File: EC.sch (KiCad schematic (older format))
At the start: 9 parts, among them J2 MICROSD, J8 DEBUG, Q3 2N7002

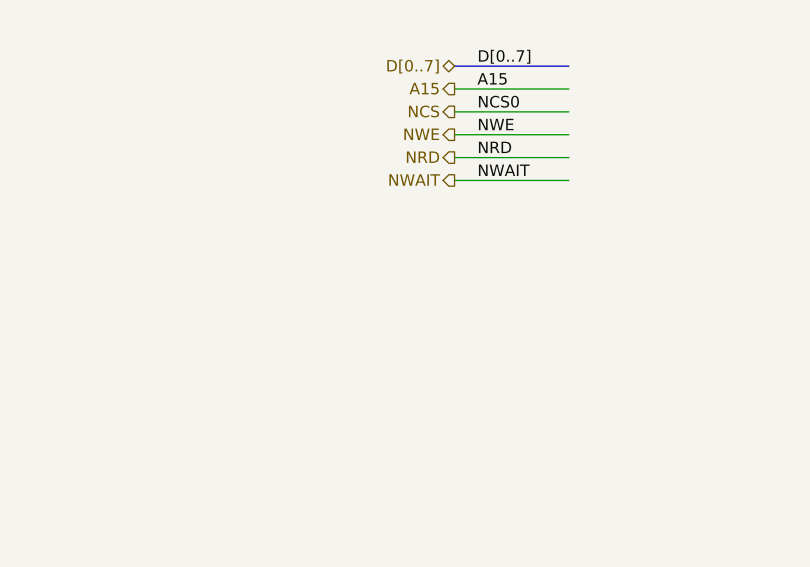
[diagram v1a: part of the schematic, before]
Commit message: Route CPU bus and cache
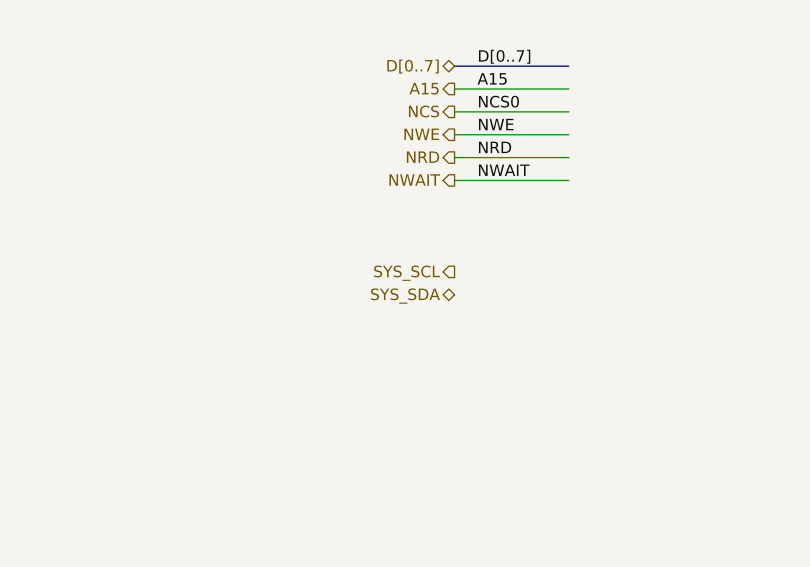
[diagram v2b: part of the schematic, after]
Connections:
- net labels added: SYS_SCL, SYS_SDA
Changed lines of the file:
@@
 $Descr A4 11693 8268
 encoding utf-8
-Sheet 7 9
+Sheet 6 9
 Title ""
 Date ""
@@
 Connection ~ 6800 1400
 $Comp
-L GND #PWR108
+L GND #PWR118
 U 1 1 577B8084
 P 6800 1500
-F 0 "#PWR108" H 6800 1500 30  0001 C CNN
+F 0 "#PWR118" H 6800 1500 30  0001 C CNN
 F 1 "GND" H 6800 1430 30  0001 C CNN
 F 2 "" H 6800 1500 60  0000 C CNN
@@
 $EndComp
 $Comp
-L GND #PWR109
+L GND #PWR119
 U 1 1 577B80BD
 P 7400 2400
-F 0 "#PWR109" H 7400 2400 30  0001 C CNN
+F 0 "#PWR119" H 7400 2400 30  0001 C CNN
 F 1 "GND" H 7400 2330 30  0001 C CNN
 F 2 "" H 7400 2400 60  0000 C CNN
@@
 	7000 1100 7000 1850
 Connection ~ 7000 1100
-$Comp
-L 2N7002 Q3
-U 1 1 577AFC0B
-P 8050 850
-F 0 "Q3" H 8177 896 50  0000 L CNN
-F 1 "2N7002" H 8177 805 50  0000 L CNN
-F 2 "smd-semi:SOT-23" H 8050 700 50  0001 C CNN
-F 3 "" H 8050 850 60  0000 C CNN
-F 4 "NMOS 2N7002" H 8050 600 60  0001 C CNN "BOM"
-	1    8050 850
-	1    0    0    -1
-$EndComp
 Text GLabel 7950 700  0    50   Input ~ 0
 3V3_LIMB
@@
 	8100 950  8100 1200
 $Comp
-L GND #PWR110
+L GND #PWR120
 U 1 1 577B0609
 P 8100 1450
-F 0 "#PWR110" H 8100 1450 30  0001 C CNN
+F 0 "#PWR120" H 8100 1450 30  0001 C CNN
 F 1 "GND" H 8100 1380 30  0001 C CNN
 F 2 "" H 8100 1450 60  0000 C CNN
@@
 	10600 5800 10500 5800
 $Comp
-L GND #PWR111
+L GND #PWR121
 U 1 1 577EAB82
 P 10600 6800
-F 0 "#PWR111" H 10600 6800 30  0001 C CNN
+F 0 "#PWR121" H 10600 6800 30  0001 C CNN
 F 1 "GND" H 10600 6730 30  0001 C CNN
 F 2 "" H 10600 6800 60  0000 C CNN
@@
 $EndComp
 $Comp
-L GND #PWR106
+L GND #PWR116
 U 1 1 577EDCE7
 P 2800 3800
-F 0 "#PWR106" H 2800 3800 30  0001 C CNN
+F 0 "#PWR116" H 2800 3800 30  0001 C CNN
 F 1 "GND" H 2800 3730 30  0001 C CNN
 F 2 "" H 2800 3800 60  0000 C CNN
@@
 	3100 3300 2700 3300
 $Comp
-L GND #PWR105
+L GND #PWR115
 U 1 1 577EDF0A
 P 2800 3100
-F 0 "#PWR105" H 2800 3100 30  0001 C CNN
+F 0 "#PWR115" H 2800 3100 30  0001 C CNN
 F 1 "GND" H 2800 3030 30  0001 C CNN
 F 2 "" H 2800 3100 60  0000 C CNN
@@
 Connection ~ 3800 2900
 $Comp
-L GND #PWR107
+L GND #PWR117
 U 1 1 577EEC84
 P 3800 3300
-F 0 "#PWR107" H 3800 3300 30  0001 C CNN
+F 0 "#PWR117" H 3800 3300 30  0001 C CNN
 F 1 "GND" H 3800 3230 30  0001 C CNN
 F 2 "" H 3800 3300 60  0000 C CNN
@@
 Wire Wire Line
 	6700 4100 6200 4100
+$Comp
+L 2N7002 Q3
+U 1 1 577AFC0B
+P 8050 850
+F 0 "Q3" H 8177 896 50  0000 L CNN
+F 1 "2N7002" H 8177 805 50  0000 L CNN
+F 2 "smd-semi:SOT-23" H 8050 700 50  0001 C CNN
+F 3 "" H 8050 850 60  0000 C CNN
+F 4 "NMOS 2N7002" H 8050 600 60  0001 C CNN "BOM"
+	1    8050 850
+	1    0    0    -1
+$EndComp
+Text HLabel 6200 4500 0    50   Output ~ 0
+SYS_SCL
+Text HLabel 6200 4600 0    50   BiDi ~ 0
+SYS_SDA
 $EndSCHEMATC

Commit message: workworkwork
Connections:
- net labels added: P3V3_STBY
- net labels removed: 3V3_LIMB
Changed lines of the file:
@@
 $Descr A4 11693 8268
 encoding utf-8
-Sheet 6 9
+Sheet 6 10
 Title ""
 Date ""
@@
 Connection ~ 7000 1100
 Text GLabel 7950 700  0    50   Input ~ 0
-3V3_LIMB
+P3V3_STBY
 Wire Wire Line
 	7950 700  8100 700
@@
 Connection ~ 10600 6700
 Text GLabel 9100 1400 0    50   Input ~ 0
-3V3_LIMB
+P3V3_STBY
 Wire Wire Line
 	9100 1400 9300 1400

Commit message: TODO: learn to write good commit messages
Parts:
- added J6: DEBUG, conn-100mil:CONN-100MIL-M-2x5-SHROUD, symbol CONN-100MIL-M-2x5-SHROUD
- added Q12, Q13: FK3303010L, manuf:PANASONIC-SSSMini3-F2-B, symbol FK3303010L
- added R17: 24, IPC7351-Nominal:RESC1005X40, symbol R-0402
- added R55, R8, R86, R9: 5k1, IPC7351-Nominal:RESC1005X40, symbol R-0402
- added SW3: SW-DIP-4, dip-sip:DIP-8, symbol SW-DIP-4
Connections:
- net labels added: BTN_AUX, BTN_PWR, FPGA_CCLK, FPGA_DATA, FPGA_DONE0, FPGA_DONE1, FPGA_DONE2, LED_ACT, LED_PWR, MISO, MOSI, NPCS0, NPCS1, NPCS2, P3V3_AUX, REQ, SCLK, SYS_SCL_S0, SYS_SCL_S5, SYS_SDA_S0, SYS_SDA_S5, TCK, TDI, TDO, TMS, ~FPGA_INIT, ~PROGRAM0, ~PROGRAM1, ~PROGRAM2, ~RST
- net labels removed: NCS2, SCK0, SDA0, SYS_SCL, SYS_SDA
- wire segments 107 -> 152
- no-connect marks 0 -> 2

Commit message: Route clocks
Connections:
- net labels added: CLK
- net labels removed: XIN
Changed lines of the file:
@@
 $Descr A4 11693 8268
 encoding utf-8
-Sheet 6 10
+Sheet 5 10
 Title ""
 Date ""
@@
 Connection ~ 6800 1400
 $Comp
-L GND #PWR128
+L GND #PWR126
 U 1 1 577B8084
 P 6800 1500
-F 0 "#PWR128" H 6800 1500 30  0001 C CNN
+F 0 "#PWR126" H 6800 1500 30  0001 C CNN
 F 1 "GND" H 6800 1430 30  0001 C CNN
 F 2 "" H 6800 1500 60  0000 C CNN
@@
 $EndComp
 $Comp
-L GND #PWR129
+L GND #PWR127
 U 1 1 577B80BD
 P 7400 2400
-F 0 "#PWR129" H 7400 2400 30  0001 C CNN
+F 0 "#PWR127" H 7400 2400 30  0001 C CNN
 F 1 "GND" H 7400 2330 30  0001 C CNN
 F 2 "" H 7400 2400 60  0000 C CNN
@@
 	8100 950  8100 1200
 $Comp
-L GND #PWR130
+L GND #PWR128
 U 1 1 577B0609
 P 8100 1450
-F 0 "#PWR130" H 8100 1450 30  0001 C CNN
+F 0 "#PWR128" H 8100 1450 30  0001 C CNN
 F 1 "GND" H 8100 1380 30  0001 C CNN
 F 2 "" H 8100 1450 60  0000 C CNN
@@
 Text Label 10600 5700 0    50   ~ 0
 USB_D-
-Text Label 10600 5600 0    50   ~ 0
-XIN
 Text Label 10600 5500 0    50   ~ 0
 XOUT
@@
 	10600 5500 10500 5500
 Wire Wire Line
-	10600 5600 10500 5600
+	10500 5600 10900 5600
 Wire Wire Line
 	10600 5700 10500 5700
@@
 	10600 5800 10500 5800
 $Comp
-L GND #PWR131
+L GND #PWR129
 U 1 1 577EAB82
 P 10600 6800
-F 0 "#PWR131" H 10600 6800 30  0001 C CNN
+F 0 "#PWR129" H 10600 6800 30  0001 C CNN
 F 1 "GND" H 10600 6730 30  0001 C CNN
 F 2 "" H 10600 6800 60  0000 C CNN
@@
 $EndComp
 $Comp
-L GND #PWR125
+L GND #PWR123
 U 1 1 577EDCE7
 P 2800 3800
-F 0 "#PWR125" H 2800 3800 30  0001 C CNN
+F 0 "#PWR123" H 2800 3800 30  0001 C CNN
 F 1 "GND" H 2800 3730 30  0001 C CNN
 F 2 "" H 2800 3800 60  0000 C CNN
@@
 	3100 3300 2700 3300
 $Comp
-L GND #PWR124
+L GND #PWR122
 U 1 1 577EDF0A
 P 2800 3100
-F 0 "#PWR124" H 2800 3100 30  0001 C CNN
+F 0 "#PWR122" H 2800 3100 30  0001 C CNN
 F 1 "GND" H 2800 3030 30  0001 C CNN
 F 2 "" H 2800 3100 60  0000 C CNN
@@
 Connection ~ 3800 2900
 $Comp
-L GND #PWR127
+L GND #PWR125
 U 1 1 577EEC84
 P 3800 3300
-F 0 "#PWR127" H 3800 3300 30  0001 C CNN
+F 0 "#PWR125" H 3800 3300 30  0001 C CNN
 F 1 "GND" H 3800 3230 30  0001 C CNN
 F 2 "" H 3800 3300 60  0000 C CNN
@@
 	2900 6600 2600 6600
 $Comp
-L GND #PWR123
+L GND #PWR121
 U 1 1 579F6A32
 P 2100 6700
-F 0 "#PWR123" H 2100 6700 30  0001 C CNN
+F 0 "#PWR121" H 2100 6700 30  0001 C CNN
 F 1 "GND" H 2100 6630 30  0001 C CNN
 F 2 "" H 2100 6700 60  0000 C CNN
@@
 	2800 4600 2800 5000
 $Comp
-L GND #PWR126
+L GND #PWR124
 U 1 1 579E34CD
 P 2800 5000
-F 0 "#PWR126" H 2800 5000 30  0001 C CNN
+F 0 "#PWR124" H 2800 5000 30  0001 C CNN
 F 1 "GND" H 2800 4930 30  0001 C CNN
 F 2 "" H 2800 5000 60  0000 C CNN
@@
 	0    1    1    0
 $EndComp
+Text HLabel 10900 5600 2    50   Input ~ 0
+CLK
 $EndSCHEMATC

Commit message: Change USB input circuit
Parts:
- removed DZ1: DRTR5V0U2SR, smd-semi:SOT-143, symbol DRTR5V0U2SR
- removed Q3: 2N7002, smd-semi:SOT-23, symbol 2N7002
- removed R3: 100k, IPC7351-Nominal:RESC1608X50, symbol R-0603
- removed R4: 10k, IPC7351-Nominal:RESC1608X50, symbol R-0603
- added Q3: FK3303010L, manuf:PANASONIC-SSSMini3-F2-B, symbol FK3303010L
- added R3: 5k1, IPC7351-Nominal:RESC1005X40, symbol R-0402
- added R4, R92, R93: 100k, IPC7351-Nominal:RESC1005X40, symbol R-0402
- added U9: NUF2042XV6, smd-semi:SOT-563, symbol NUF2042XV6
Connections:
- net labels added: OUT_USB1_D+, OUT_USB1_D-
- wire segments 152 -> 155
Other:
- moved on the sheet: J8
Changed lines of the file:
@@
 L CONN-10118194-0001LF-UUSB-B J8
 U 1 1 5766048A
-P 6500 1100
-F 0 "J8" H 6677 1120 50  0000 L CNN
-F 1 "DEBUG" H 6677 1029 50  0000 L CNN
-F 2 "conn-fci:CONN-10118194-0001LF-FCI" H 6500 1100 50  0001 C CNN
-F 3 "" H 6400 1300 50  0000 C CNN
-F 4 "DIST DIGIKEY 609-4618-1-ND" H 7000 2000 50  0001 C CNN "BOM"
-	1    6500 1100
+P 2300 1500
+F 0 "J8" H 2477 1520 50  0000 L CNN
+F 1 "DEBUG" H 2477 1429 50  0000 L CNN
+F 2 "conn-fci:CONN-10118194-0001LF-FCI" H 2300 1500 50  0001 C CNN
+F 3 "" H 2200 1700 50  0000 C CNN
+F 4 "DIST DIGIKEY 609-4618-1-ND" H 2800 2400 50  0001 C CNN "BOM"
+	1    2300 1500
 	-1   0    0    -1
 $EndComp
 Text Notes 600  700  0    50   ~ 0
 Local Integrated Management Bits - EC
-$Comp
-L DRTR5V0U2SR DZ1
-U 1 1 577B7FBC
-P 7400 1900
-F 0 "DZ1" H 7170 1946 50  0000 R CNN
-F 1 "DRTR5V0U2SR" H 7170 1855 50  0000 R CNN
-F 2 "smd-semi:SOT-143" H 7400 1400 60  0001 C CNN
-F 3 "" H 7400 1850 60  0000 C CNN
-F 4 "TVS DIODESINC DRTR5V0U2SR" H 7400 1300 60  0001 C CNN "BOM"
-	1    7400 1900
-	-1   0    0    -1
-$EndComp
-Wire Wire Line
-	6700 900  8000 900
-Wire Wire Line
-	7400 900  7400 1500
-Wire Wire Line
-	6700 1000 7800 1000
-Wire Wire Line
-	7000 1850 7100 1850
-Wire Wire Line
-	7100 1950 6900 1950
-Wire Wire Line
-	6700 1100 7800 1100
-Wire Wire Line
-	6700 1300 6800 1300
-Wire Wire Line
-	6800 1300 6800 1500
-Wire Wire Line
-	6800 1400 6750 1400
-Connection ~ 6800 1400
-$Comp
-L GND #PWR126
-U 1 1 577B8084
-P 6800 1500
-F 0 "#PWR126" H 6800 1500 30  0001 C CNN
-F 1 "GND" H 6800 1430 30  0001 C CNN
-F 2 "" H 6800 1500 60  0000 C CNN
-F 3 "" H 6800 1500 60  0000 C CNN
-	1    6800 1500
-	-1   0    0    -1
-$EndComp
-$Comp
-L GND #PWR127
-U 1 1 577B80BD
-P 7400 2400
-F 0 "#PWR127" H 7400 2400 30  0001 C CNN
-F 1 "GND" H 7400 2330 30  0001 C CNN
-F 2 "" H 7400 2400 60  0000 C CNN
-F 3 "" H 7400 2400 60  0000 C CNN
-	1    7400 2400
-	-1   0    0    -1
-$EndComp
-Wire Wire Line
-	7400 2400 7400 2300
-Text Label 7800 1000 2    50   ~ 0
+Text Label 4800 1500 2    50   ~ 0
 USB_D+
-Text Label 7800 1100 2    50   ~ 0
+Text Label 4800 1400 2    50   ~ 0
 USB_D-
-Text Label 9100 1100 2    50   ~ 0
+Text Label 6050 1050 2    50   ~ 0
 USB_VBUS
-Connection ~ 7400 900
-Wire Wire Line
-	6900 1950 6900 1000
-Connection ~ 6900 1000
-Wire Wire Line
-	7000 1100 7000 1850
-Connection ~ 7000 1100
-Text GLabel 7950 700  0    50   Input ~ 0
+Text GLabel 4900 650  0    50   Input ~ 0
 P3V3_STBY
-Wire Wire Line
-	7950 700  8100 700
-Wire Wire Line
-	8100 700  8100 750
-$Comp
-L R-0603 R3
-U 1 1 577B0535
-P 8100 1300
-F 0 "R3" H 8163 1346 50  0000 L CNN
-F 1 "100k" H 8163 1255 50  0000 L CNN
-F 2 "IPC7351-Nominal:RESC1608X50" H 8100 1300 50  0001 C CNN
-F 3 "" H 8100 1350 60  0000 C CNN
-F 4 "RES SMD 100k 1% [0603]" H 8850 1850 60  0001 C CNN "BOM"
-	1    8100 1300
-	1    0    0    -1
-$EndComp
-Wire Wire Line
-	8100 950  8100 1200
-$Comp
-L GND #PWR128
-U 1 1 577B0609
-P 8100 1450
-F 0 "#PWR128" H 8100 1450 30  0001 C CNN
-F 1 "GND" H 8100 1380 30  0001 C CNN
-F 2 "" H 8100 1450 60  0000 C CNN
-F 3 "" H 8100 1450 60  0000 C CNN
-	1    8100 1450
-	1    0    0    -1
-$EndComp
-Wire Wire Line
-	8100 1450 8100 1400
-$Comp
-L R-0603 R4
-U 1 1 577B0648
-P 8500 1100
-F 0 "R4" V 8608 1100 50  0000 C CNN
-F 1 "10k" V 8699 1100 50  0000 C CNN
-F 2 "IPC7351-Nominal:RESC1608X50" H 8500 1100 50  0001 C CNN
-F 3 "" H 8500 1150 60  0000 C CNN
-F 4 "RES SMD 10k 1% [0603]" H 9250 1650 60  0001 C CNN "BOM"
-	1    8500 1100
-	0    1    1    0
-$EndComp
-Wire Wire Line
-	8400 1100 8100 1100
-Connection ~ 8100 1100
-Wire Wire Line
-	9100 1100 8600 1100
 $Comp
 L ATSAM4S16CA-AU LIMB1
@@
 $EndComp
 $Comp
-L GND #PWR123
+L GND #PWR124
 U 1 1 577EDCE7
 P 2800 3800
-F 0 "#PWR123" H 2800 3800 30  0001 C CNN
+F 0 "#PWR124" H 2800 3800 30  0001 C CNN
 F 1 "GND" H 2800 3730 30  0001 C CNN
 F 2 "" H 2800 3800 60  0000 C CNN
@@
 	3100 3300 2700 3300
 $Comp
-L GND #PWR122
+L GND #PWR123
 U 1 1 577EDF0A
 P 2800 3100
-F 0 "#PWR122" H 2800 3100 30  0001 C CNN
+F 0 "#PWR123" H 2800 3100 30  0001 C CNN
 F 1 "GND" H 2800 3030 30  0001 C CNN
 F 2 "" H 2800 3100 60  0000 C CNN
@@
 Connection ~ 3800 2900
 $Comp
-L GND #PWR125
+L GND #PWR127
 U 1 1 577EEC84
 P 3800 3300
-F 0 "#PWR125" H 3800 3300 30  0001 C CNN
+F 0 "#PWR127" H 3800 3300 30  0001 C CNN
 F 1 "GND" H 3800 3230 30  0001 C CNN
 F 2 "" H 3800 3300 60  0000 C CNN
@@
 Wire Wire Line
 	2900 5900 2400 5900
-$Comp
-L 2N7002 Q3
-U 1 1 577AFC0B
-P 8050 850
-F 0 "Q3" H 8177 896 50  0000 L CNN
-F 1 "2N7002" H 8177 805 50  0000 L CNN
-F 2 "smd-semi:SOT-23" H 8050 700 50  0001 C CNN
-F 3 "" H 8050 850 60  0000 C CNN
-F 4 "NMOS 2N7002" H 8050 600 60  0001 C CNN "BOM"
-	1    8050 850
-	1    0    0    -1
-$EndComp
 Text HLabel 6100 4000 0    50   Output ~ 0
 SYS_SCL_S5
@@
 	2800 4600 2800 5000
 $Comp
-L GND #PWR124
+L GND #PWR125
 U 1 1 579E34CD
 P 2800 5000
-F 0 "#PWR124" H 2800 5000 30  0001 C CNN
+F 0 "#PWR125" H 2800 5000 30  0001 C CNN
 F 1 "GND" H 2800 4930 30  0001 C CNN
 F 2 "" H 2800 5000 60  0000 C CNN
@@
 Text HLabel 10900 5600 2    50   Input ~ 0
 CLK
+$Comp
+L NUF2042XV6 U9
+U 1 1 57A167C2
+P 3600 1600
+F 0 "U9" H 3600 2167 50  0000 C CNN
+F 1 "NUF2042XV6" H 3600 2076 50  0000 C CNN
+F 2 "smd-semi:SOT-563" H 3600 900 50  0001 C CNN
+F 3 "http://www.onsemi.com/pub_link/Collateral/NUF2030XV6-D.PDF" H 3600 1100 50  0001 C CNN
+F 4 "IC ONSEMI NUF2042XV6" H 3600 1000 60  0001 C CNN "BOM"
+	1    3600 1600
+	1    0    0    -1
+$EndComp
+Wire Wire Line
+	2500 1400 2900 1400
+Wire Wire Line
+	2900 1500 2500 1500
+Wire Wire Line
+	2500 1700 2800 1700
+Wire Wire Line
+	2800 1700 2800 2000
+Wire Wire Line
+	2800 1900 2900 1900
+Connection ~ 2800 1900
+$Comp
+L GND #PWR122
+U 1 1 57A16E2F
+P 2800 2000
+F 0 "#PWR122" H 2800 2000 30  0001 C CNN
+F 1 "GND" H 2800 1930 30  0001 C CNN
+F 2 "" H 2800 2000 60  0000 C CNN
+F 3 "" H 2800 2000 60  0000 C CNN
+	1    2800 2000
+	1    0    0    -1
+$EndComp
+Wire Wire Line
+	2500 1300 2800 1300
+Wire Wire Line
+	2800 1300 2800 900
+Wire Wire Line
+	2800 900  4550 900
+$Comp
+L R-0402 R4
+U 1 1 57A170BF
+P 4650 900
+F 0 "R4" V 4758 900 50  0000 C CNN
+F 1 "100k" V 4849 900 50  0000 C CNN
+F 2 "IPC7351-Nominal:RESC1005X40" H 4650 900 50  0001 C CNN
+F 3 "" H 4650 950 60  0000 C CNN
+F 4 "RES SMD 100k 1% [0402]" H 5400 1450 60  0001 C CNN "BOM"
+	1    4650 900
+	0    1    1    0
+$EndComp
+$Comp
+L R-0402 R3
+U 1 1 57A171B1
+P 2900 1100
+F 0 "R3" H 2837 1054 50  0000 R CNN
+F 1 "5k1" H 2837 1145 50  0000 R CNN
+F 2 "IPC7351-Nominal:RESC1005X40" H 2900 1100 50  0001 C CNN
+F 3 "" H 2900 1150 60  0000 C CNN
+F 4 "RES SMD 5k1 1% [0402]" H 3650 1650 60  0001 C CNN "BOM"
+	1    2900 1100
+	-1   0    0    1
+$EndComp
+Wire Wire Line
+	2900 1000 2900 900
+Connection ~ 2900 900
+$Comp
+L GND #PWR126
+U 1 1 57A172F2
+P 2900 1250
+F 0 "#PWR126" H 2900 1250 30  0001 C CNN
+F 1 "GND" H 2900 1180 30  0001 C CNN
+F 2 "" H 2900 1250 60  0000 C CNN
+F 3 "" H 2900 1250 60  0000 C CNN
+	1    2900 1250
+	1    0    0    -1
+$EndComp
+Wire Wire Line
+	2900 1250 2900 1200
+Wire Wire Line
+	4400 900  4400 1300
+Wire Wire Line
+	4400 1300 4300 1300
+Wire Wire Line
+	4800 1500 4300 1500
+Wire Wire Line
+	4300 1400 4800 1400
+$Comp
+L FK3303010L Q3
+U 1 1 57A17871
+P 4950 850
+F 0 "Q3" H 5077 896 50  0000 L CNN
+F 1 "FK3303010L" H 5077 805 50  0000 L CNN
+F 2 "manuf:PANASONIC-SSSMini3-F2-B" H 4950 700 50  0001 C CNN
+F 3 "" H 4950 850 60  0000 C CNN
+F 4 "NMOS Panasonic FK3303010L" H 4950 600 60  0001 C CNN "BOM"
+	1    4950 850
+	1    0    0    -1
+$EndComp
+Connection ~ 4400 900
+Wire Wire Line
+	4900 650  5000 650
+Wire Wire Line
+	5000 650  5000 750
+$Comp
+L R-0402 R92
+U 1 1 57A17D7C
+P 5000 1200
+F 0 "R92" H 4937 1154 50  0000 R CNN
+F 1 "100k" H 4937 1245 50  0000 R CNN
+F 2 "IPC7351-Nominal:RESC1005X40" H 5000 1200 50  0001 C CNN
+F 3 "" H 5000 1250 60  0000 C CNN
+F 4 "RES SMD 100k 1% [0402]" H 5750 1750 60  0001 C CNN "BOM"
+	1    5000 1200
+	-1   0    0    1
+$EndComp
+Wire Wire Line
+	5000 1100 5000 950
+$Comp
+L GND #PWR128
+U 1 1 57A17F1F
+P 5000 1350
+F 0 "#PWR128" H 5000 1350 30  0001 C CNN
+F 1 "GND" H 5000 1280 30  0001 C CNN
+F 2 "" H 5000 1350 60  0000 C CNN
+F 3 "" H 5000 1350 60  0000 C CNN
+	1    5000 1350
+	1    0    0    -1
+$EndComp
+Wire Wire Line
+	5000 1300 5000 1350
+$Comp
+L R-0402 R93
+U 1 1 57A18081
+P 5450 1050
+F 0 "R93" V 5342 1050 50  0000 C CNN
+F 1 "100k" V 5251 1050 50  0000 C CNN
+F 2 "IPC7351-Nominal:RESC1005X40" H 5450 1050 50  0001 C CNN
+F 3 "" H 5450 1100 60  0000 C CNN
+F 4 "RES SMD 100k 1% [0402]" H 6200 1600 60  0001 C CNN "BOM"
+	1    5450 1050
+	0    -1   -1   0
+$EndComp
+Wire Wire Line
+	5350 1050 5000 1050
+Connection ~ 5000 1050
+Wire Wire Line
+	6050 1050 5550 1050
+Text Label 2550 1400 0    50   ~ 0
+OUT_USB1_D-
+Text Label 2550 1500 0    50   ~ 0
+OUT_USB1_D+
+Wire Wire Line
+	4900 900  4750 900
 $EndSCHEMATC

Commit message: Add RS-232
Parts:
- removed Q3: FK3303010L, manuf:PANASONIC-SSSMini3-F2-B, symbol FK3303010L
- removed R92, R93: 100k, IPC7351-Nominal:RESC1005X40, symbol R-0402
- added C125, C126, C127, C128, C129: 100n, IPC7351-Nominal:CAPC1005X55, symbol C-0402
- added J10: RS232, symbol CONN-100MIL-M-1x9
- added R87, R92, R93, R94: 22V, IPC7351-Nominal:RESC1608X50, symbol VARISTOR
- added U10: MAX3232PW, IPC7351-Nominal:SOP65P640X140-16, symbol MAX3232PW
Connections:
- net labels added: CTS1, RSCTS, RSDCD, RSDSR, RSDTR, RSRD, RSRI, RSRTS, RSTD, RTS1, RXD1, TXD1
- net labels removed: A20, A23
- wire segments 155 -> 191
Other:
- note removed: "Local Integrated Management Bits - EC"
- moved on the sheet: C9, J2, J8, R3, R4, R56, U9
